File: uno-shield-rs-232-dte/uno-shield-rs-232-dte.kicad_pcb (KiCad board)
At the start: 2 copper layers, 68.6 x 53.3 mm, 20 parts, among them J1 Ctrl Route, J3 DSR/CTS, J4 DB9_Male, P1 Power, P2 Analog, P3 Digital, P4 Digital, P5 CONN_01X01, P7 CONN_01X01, U1 MAX232

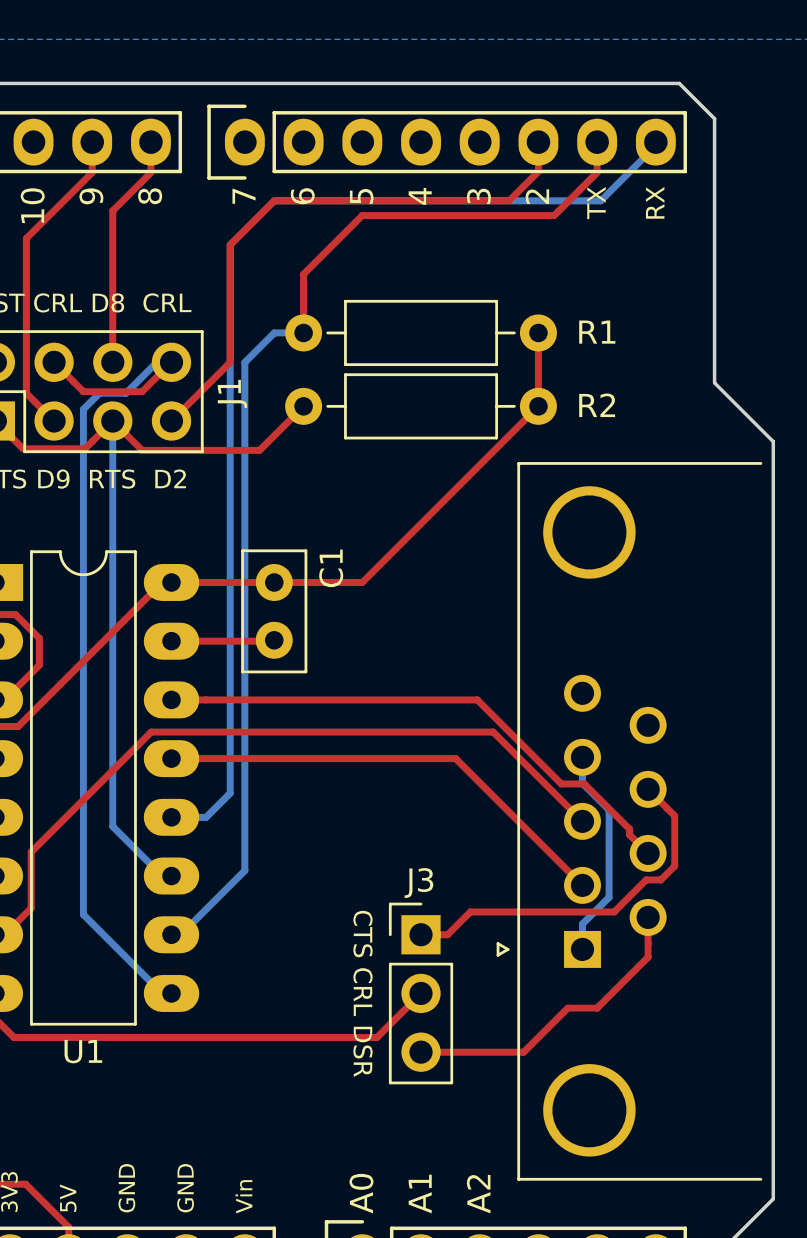
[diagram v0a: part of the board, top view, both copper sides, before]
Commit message: Adjust DTE shield to allow UART routing.
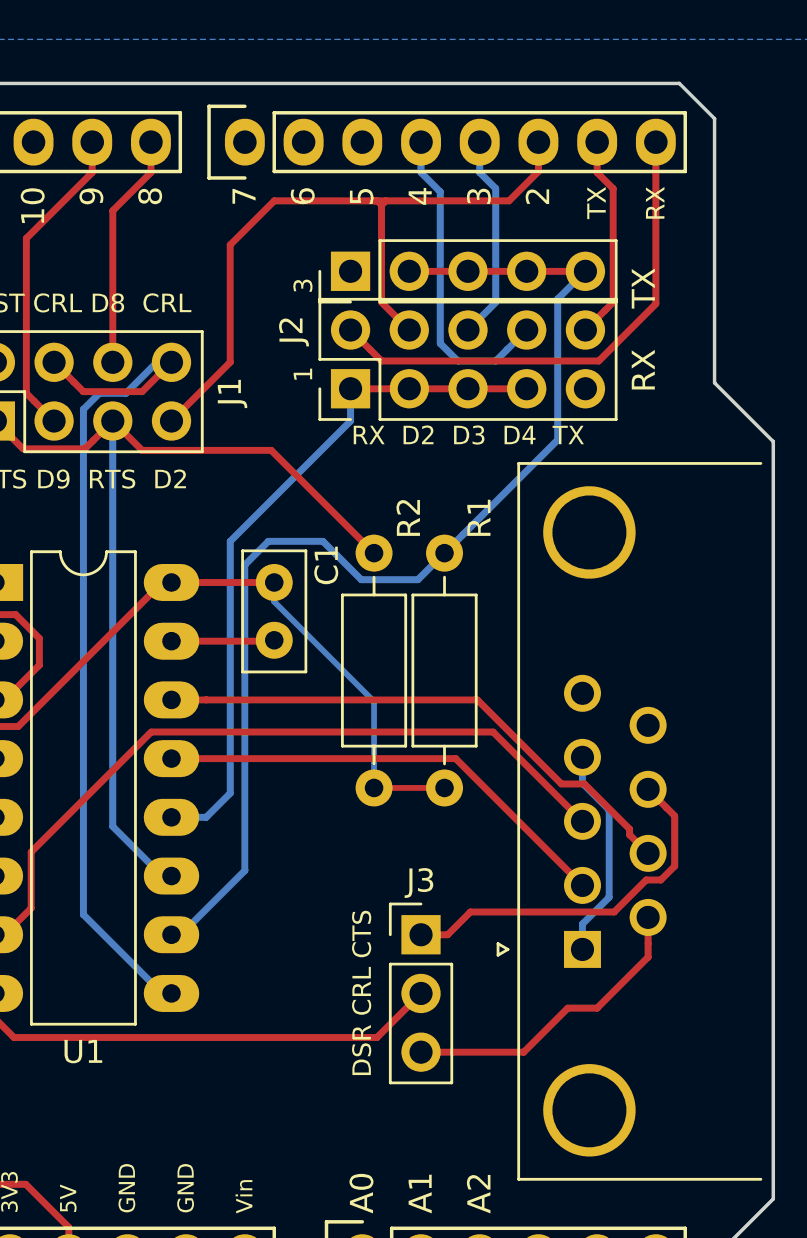
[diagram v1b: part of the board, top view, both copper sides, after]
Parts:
- added J2: RX Route, Connector_PinHeader_2.54mm:PinHeader_2x05_P2.54mm_Vertical, F.Cu at (161.3, 86.2)
- added J5: TX Route, Connector_PinHeader_2.54mm:PinHeader_1x05_P2.54mm_Vertical, F.Cu at (161.3, 81.2)
- moved R1 20.1 mm to (165.4, 103.5), turned to 90 degrees
- moved R2 18.0 mm to (162.3, 103.5), turned to 90 degrees
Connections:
- P4 pad 4: /4 -> D4
- P4 pad 5: /3(**) -> D3
- R1 pad 2: TX -> UTX
- U1 pad 10: TX -> UTX
- U1 pad 12: RX -> URX
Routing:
- net UTX: track 0.00 -> 50.1 mm
- net TX: track 47.8 -> 8.91 mm
- net URX: track 0.00 -> 30.2 mm
- net RX: track 47.0 -> 21.9 mm
- net D4: track 0.00 -> 13.7 mm
- net D3: track 0.00 -> 8.91 mm
- net D2: track 24.6 -> 31.2 mm
- net /URTS: track 36.6 -> 40.7 mm
- net +5V: track 79.1 -> 75.0 mm
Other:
- board text added: "1 3"
- board text added: "DSR CRL CTS"
- board text added: "RX D2 D3 D4 TX"
- board text added: "RX TX"
- board text removed: "CTS CRL DSR"
